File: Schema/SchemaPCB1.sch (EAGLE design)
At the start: 17 parts, among them IC1 ESP32-WROOM-32E_M113EH3200PH3Q, IC2 CP2101-GM, J1 10104110-0001LF

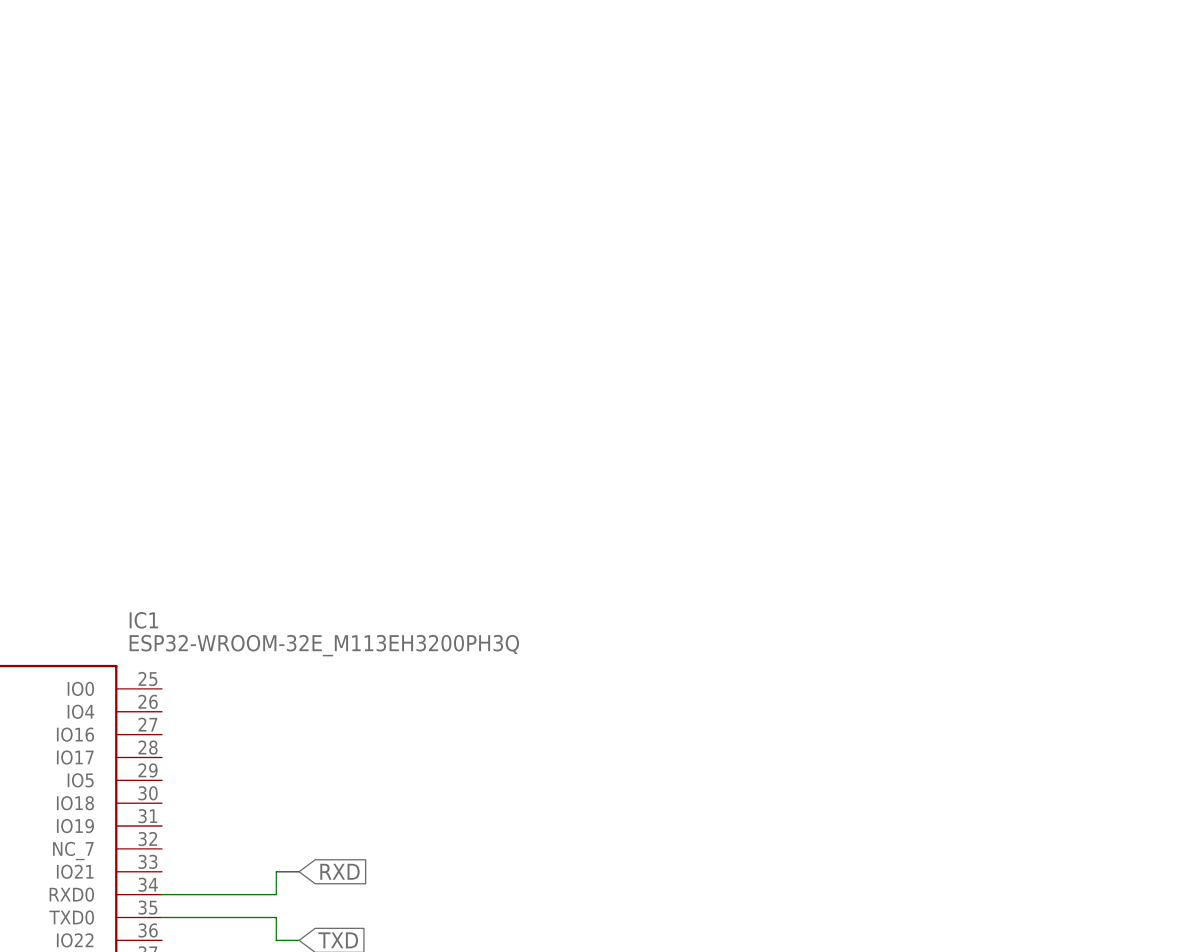
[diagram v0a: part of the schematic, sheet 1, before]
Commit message: LoRa toegevoegd
RN2483 en power voorziening voor de RN2483 aangebracht op het schema
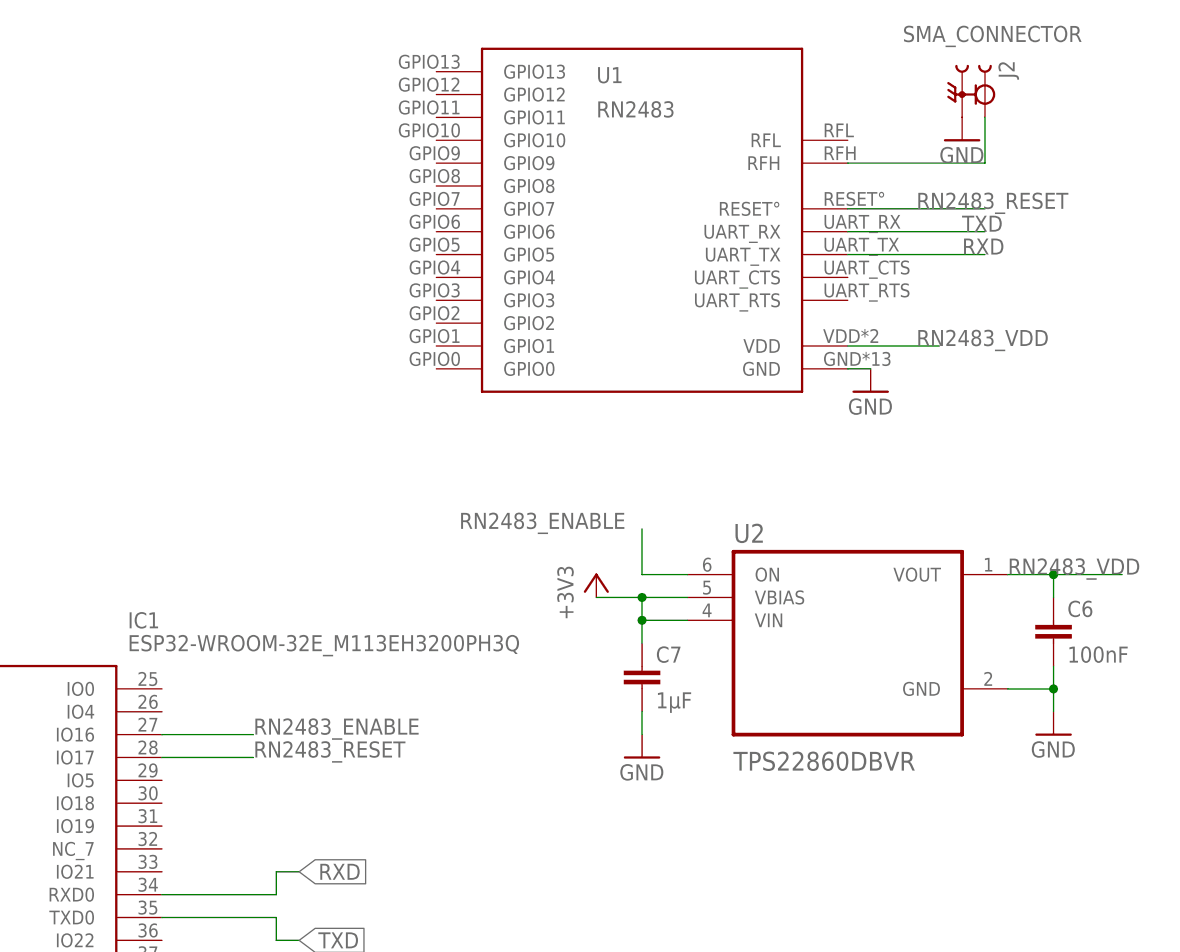
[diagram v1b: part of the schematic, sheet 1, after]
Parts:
- added C6: 100nF, --CoolTeamLib:C-EUC0805
- added C7: 1µF, --CoolTeamLib:C-EUC0805
- added J2: SMA_CONNECTOR, --CoolTeamLib:SMA_CONNECTOR
- added U1: RN2483, --CoolTeamLib:RN2483
- added U2: TPS22860DBVR, --TPS22860DBVR:TPS22860DBVR
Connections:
- new net N$4: J2.1, U1.RFH
- new net RN2483_ENABLE: IC1.IO16, U2.ON
- new net RN2483_RESET: IC1.IO17, U1.RESET°
- new net RN2483_VDD: C6.1, U1.VDD, U2.VOUT
- net +3V3: now also C7.1, U2.VBIAS, U2.VIN
- net GND: now also C6.2, C7.2, J2.2, U1.GND, U2.GND
- net RXD: now also U1.UART_TX
- net TXD: now also U1.UART_RX

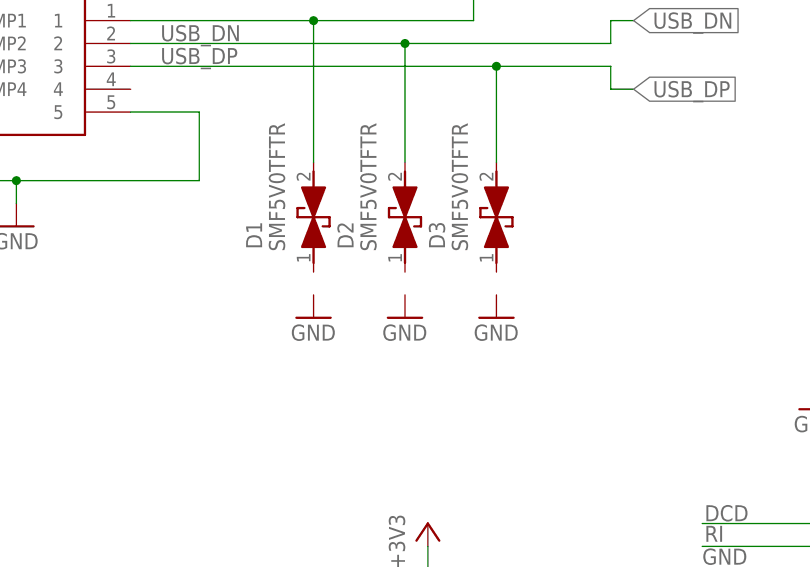
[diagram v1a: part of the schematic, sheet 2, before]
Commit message: buck bom list added
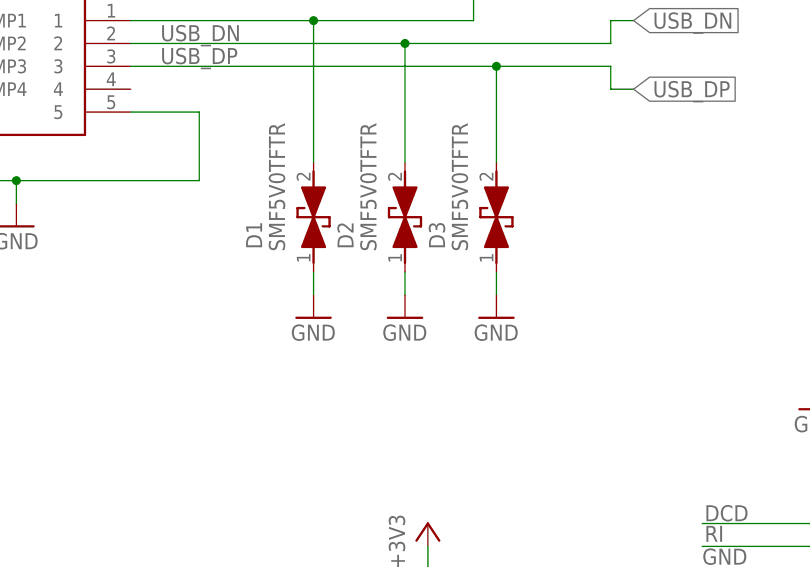
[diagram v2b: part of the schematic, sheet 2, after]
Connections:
- net GND: now also D1.K, D2.K, D3.K
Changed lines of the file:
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@@
 <junction x="50.8" y="165.1"/>
+</segment>
+<segment>
+<pinref part="D1" gate="G$1" pin="K"/>
+<pinref part="GND8" gate="1" pin="GND"/>
+<wire x1="83.82" y1="154.94" x2="83.82" y2="152.4" width="0.1524" layer="91"/>
+</segment>
+<segment>
+<pinref part="D2" gate="G$1" pin="K"/>
+<pinref part="GND9" gate="1" pin="GND"/>
+<wire x1="93.98" y1="154.94" x2="93.98" y2="152.4" width="0.1524" layer="91"/>
+</segment>
+<segment>
+<pinref part="D3" gate="G$1" pin="K"/>
+<pinref part="GND10" gate="1" pin="GND"/>
+<wire x1="104.14" y1="154.94" x2="104.14" y2="152.4" width="0.1524" layer="91"/>
 </segment>
 </net>

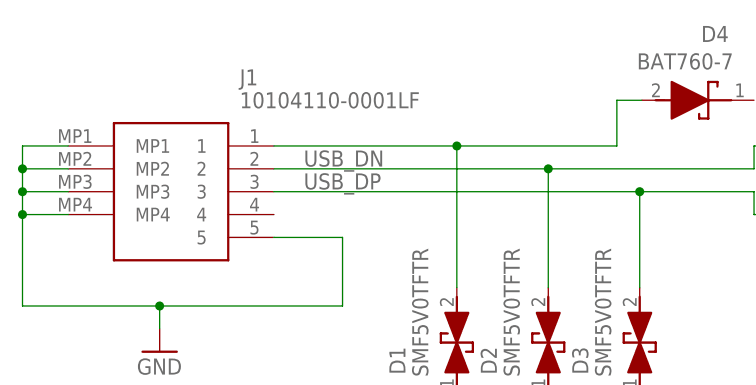
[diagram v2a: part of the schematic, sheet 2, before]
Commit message: buck added (shcema en bom)
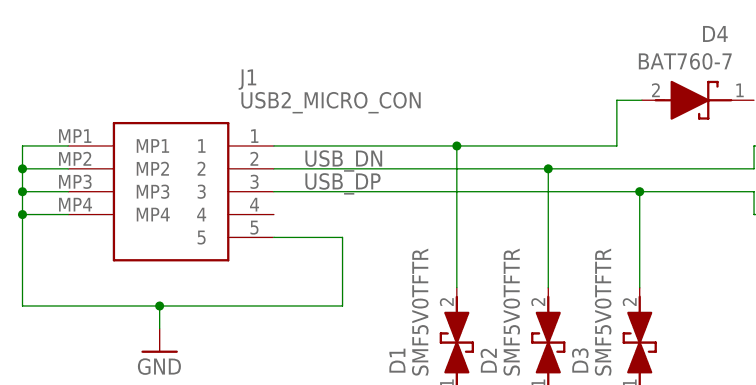
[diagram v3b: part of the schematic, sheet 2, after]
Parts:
- added CBOOT: 100nF, --CoolTeamLib:C-EU-0603C0805
- added CFF: 39pF, --CoolTeamLib:C-EU-0603C0805
- added CIN: 10µF, --CoolTeamLib:C-EU-0805C0805
- added CINX: 100nF, --CoolTeamLib:C-EU-0805C0805
- added COUT: 22µF, --CoolTeamLib:C-EU-0805C0805
- added IC3: TPS563207DRLR, --CoolTeamLib:TPS563207DRLR
- added L1: 3,3µH, --CoolTeamLib:SDR1307-3R3ML
- added R6: 30k9Û, --CoolTeamLib:R-EU_0603M0805
- added R7: 10kÛ, --CoolTeamLib:R-EU_0603M0805
- C1, C2, C4, C6, C7: device --CoolTeamLib:C-EUC0805 -> --CoolTeamLib:C-EU-0805C0805
- J1: value 10104110-0001LF -> USB2_MICRO_CON; device --CoolTeamLib:10104110-0001LF -> --CoolTeamLib:USB2_MICRO_CON
- R1, R2, R3, R4, R5: device --CoolTeamLib:R-EU_M0805 -> --CoolTeamLib:R-EU_0805M0805
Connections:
- new net 3V3: CFF.1, COUT.1, L1.2, R6.2
- new net BAT_IN: CIN.1, CINX.1, IC3.EN, IC3.VIN
- new net N$6: CBOOT.1, IC3.BST
- new net N$7: CBOOT.2, IC3.SW, L1.1
- new net N$8: CFF.2, IC3.FB, R6.1, R7.2
- net GND: now also CIN.2, CINX.2, COUT.2, IC3.GND, R7.1
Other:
- note added: "quantity 2??????"

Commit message: schemaa
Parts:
- removed CBOOT: 100nF, --CoolTeamLib:C-EU-0603C0805
- removed CFF: 39pF, --CoolTeamLib:C-EU-0603C0805
- removed CIN: 10µF, --CoolTeamLib:C-EU-0805C0805
- removed CINX: 100nF, --CoolTeamLib:C-EU-0805C0805
- removed COUT: 22µF, --CoolTeamLib:C-EU-0805C0805
- removed D1, D2, D3: SMF5V0TFTR, --CoolTeamLib:SMF5V0TFTR
- removed D4: BAT760-7, --CoolTeamLib:BAT760-7
- removed IC2: CP2101-GM, --CoolTeamLib:CP2101-GM
- removed IC3: TPS563207DRLR, --CoolTeamLib:TPS563207DRLR
- removed J1: USB2_MICRO_CON, --CoolTeamLib:USB2_MICRO_CON
- removed L1: 3,3µH, --CoolTeamLib:SDR1307-3R3ML
- removed R2: 22k1Û 5%, --CoolTeamLib:R-EU_0805M0805
- removed R3: 47k5Û 5%, --CoolTeamLib:R-EU_0805M0805
- removed R4: 2kÛ 5%, --CoolTeamLib:R-EU_0805M0805
- removed R5: 10kÛ 5%, --CoolTeamLib:R-EU_0805M0805
- removed R6: 30k9Û, --CoolTeamLib:R-EU_0603M0805
- removed R7: 10kÛ, --CoolTeamLib:R-EU_0603M0805
- added U$1: SOT-89-5, --CoolTeamLib:SOT-89-5
- C4: value 0,1µF -> (none)
- C5: value 4,7µF -> (none); device --CoolTeamLib:CPOL-EU153CLV-0605 -> --CoolTeamLib:C-EU-0805C0805
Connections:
- removed net 3V3: CFF.1, COUT.1, L1.2, R6.2
- removed net BAT_IN: CIN.1, CINX.1, IC3.EN, IC3.VIN
- removed net CTS: IC2.CTS
- removed net DCD: IC2.DCD
- removed net DSR: IC2.DSR
- removed net DTR: IC2.DTR
- removed net N$6: CBOOT.1, IC3.BST
- removed net N$7: CBOOT.2, IC3.SW, L1.1
- removed net N$8: CFF.2, IC3.FB, R6.1, R7.2
- removed net N$9: IC2.VBUS, R2.2, R3.2
- removed net RI: IC2.RI
- removed net RST: IC2.!RST, R4.2
- removed net RTS: IC2.RTS
- removed net SUSPEND: IC2.!SUSPEND, R5.2
- removed net USB_DN: D2.A, IC2.D-, J1.2
- removed net USB_DP: D3.A, IC2.D+, J1.3
- removed net VBUS: R2.1
- net +3V3: no longer C4.1, C5.+, IC2.REGIN, IC2.VDD, R4.1
- net GND: no longer C4.2, C5.-, CIN.2, CINX.2, COUT.2, D1.K, D2.K, D3.K, IC2.EP, IC2.GND, IC3.GND, J1.5, J1.MP1, J1.MP2, J1.MP3, J1.MP4, R3.1, R5.1, R7.1
- net N$3: now also U$1.VSS; no longer D1.A, D4.A, J1.1
- net RXD: no longer IC2.RXD
- net TXD: no longer IC2.TXD
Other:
- note removed: "quantity 2??????"

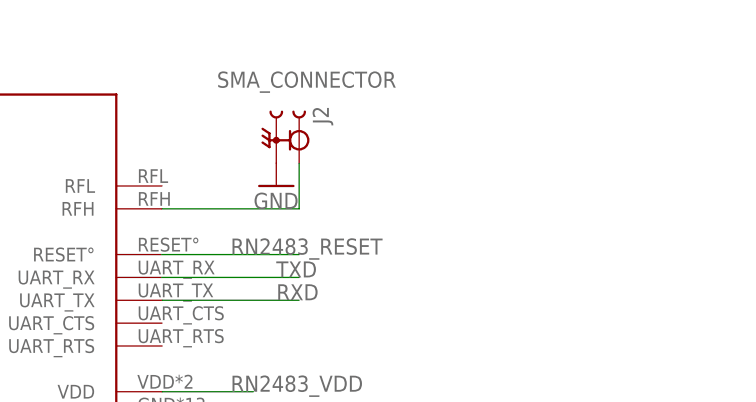
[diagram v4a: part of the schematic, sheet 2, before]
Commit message: LoRa schema afgewerkt
Klaar voor board te maken
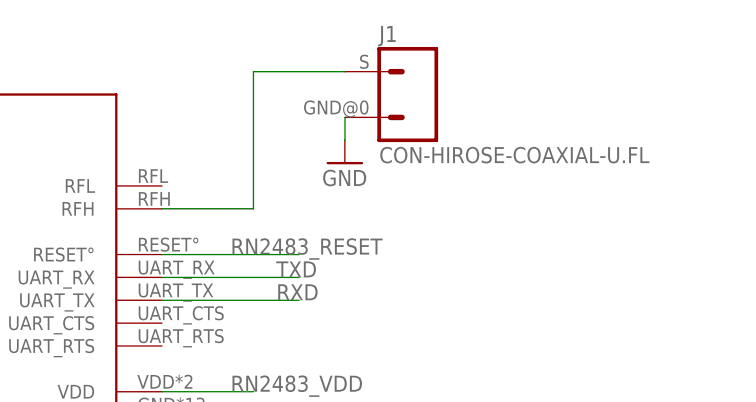
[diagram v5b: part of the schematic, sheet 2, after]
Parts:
- removed J2: SMA_CONNECTOR, --CoolTeamLib:SMA_CONNECTOR
- added J1: CON-HIROSE-COAXIAL-U.FL, --CoolTeamLib:CON-HIROSE-COAXIAL-U.FL
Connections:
- net GND: now also J1.2; no longer J2.2
- net N$4: now also J1.1; no longer J2.1
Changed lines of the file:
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@@
 <drawing>
 <settings>
-<setting alwaysvectorfont="yes"/>
+<setting alwaysvectorfont="no"/>
 <setting keepoldvectorfont="yes"/>
 <setting verticaltext="up"/>
@@
 <part name="GND12" library="supply1" library_urn="urn:adsk.eagle:library:371" deviceset="GND" device=""/>
 <part name="GND13" library="supply1" library_urn="urn:adsk.eagle:library:371" deviceset="GND" device=""/>
-<part name="J2" library="--CoolTeamLib" deviceset="SMA_CONNECTOR" device=""/>
 <part name="GND14" library="supply1" library_urn="urn:adsk.eagle:library:371" deviceset="GND" device=""/>
 <part name="FRAME3" library="frames" library_urn="urn:adsk.eagle:library:229" deviceset="FRAME_A_L" device=""/>
@@
 <part name="C4" library="--CoolTeamLib" deviceset="C-EU-0805" device="C0805" package3d_urn="urn:adsk.eagle:package:23617/2"/>
 <part name="C5" library="--CoolTeamLib" deviceset="C-EU-0805" device="C0805" package3d_urn="urn:adsk.eagle:package:23617/2"/>
+<part name="J1" library="--CoolTeamLib" deviceset="CON-HIROSE-COAXIAL" device="-U.FL"/>
 </parts>
 <sheets>
@@
 <attribute name="VALUE" x="165.1" y="76.2" size="1.778" layer="96"/>
 </instance>
-<instance part="J2" gate="G$1" x="160.02" y="149.86" smashed="yes" rot="R270">
-<attribute name="NAME" x="161.544" y="153.67" size="1.778" layer="95" rot="R270"/>
-<attribute name="VALUE" x="150.876" y="155.702" size="1.778" layer="96"/>
-</instance>
-<instance part="GND14" gate="1" x="157.48" y="144.78" smashed="yes">
-<attribute name="VALUE" x="154.94" y="142.24" size="1.778" layer="96"/>
+<instance part="GND14" gate="1" x="165.1" y="147.32" smashed="yes">
+<attribute name="VALUE" x="162.56" y="144.78" size="1.778" layer="96"/>
+</instance>
+<instance part="J1" gate="G$1" x="172.72" y="154.94" smashed="yes">
+<attribute name="VALUE" x="168.91" y="147.32" size="1.778" layer="96"/>
+<attribute name="NAME" x="168.91" y="160.782" size="1.778" layer="95"/>
 </instance>
 </instances>
@@
 </segment>
 <segment>
-<pinref part="J2" gate="G$1" pin="2"/>
 <pinref part="GND14" gate="1" pin="GND"/>
+<pinref part="J1" gate="G$1" pin="2"/>
+<wire x1="165.1" y1="149.86" x2="165.1" y2="152.4" width="0.1524" layer="91"/>
 </segment>
 </net>
@@
 <segment>
 <pinref part="U1" gate="G$1" pin="RFH"/>
-<wire x1="144.78" y1="142.24" x2="160.02" y2="142.24" width="0.1524" layer="91"/>
-<pinref part="J2" gate="G$1" pin="1"/>
-<wire x1="160.02" y1="142.24" x2="160.02" y2="147.32" width="0.1524" layer="91"/>
-</segment>
-</net>
+<wire x1="144.78" y1="142.24" x2="154.94" y2="142.24" width="0.1524" layer="91"/>
+<wire x1="154.94" y1="142.24" x2="154.94" y2="157.48" width="0.1524" layer="91"/>
+<pinref part="J1" gate="G$1" pin="1"/>
+<wire x1="154.94" y1="157.48" x2="165.1" y2="157.48" width="0.1524" layer="91"/>
+</segment>
+</net>

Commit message: schema dingen
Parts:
- added C8, C9: 100nF, --CoolTeamLib:C-EU-0805C0805
- added J2: Programmer, --CoolTeamLib:CONN_05
- added J3: (no value), --CoolTeamLib:CONN_10"
- added R2, R3: 4k6Û, --CoolTeamLib:R-EU_0805M0805
- added S1, S2: LL3301NF065QG, --CoolTeamLib:LL3301NF065QG
- added U5: SI7217-B-01-IVR, --CoolTeamLib:SI7217-B-01-IVR
- C1, C2: value 0,1µF -> 100nF
- C3: device --CoolTeamLib:CPOL-EU153CLV-0605 -> --CoolTeamLib:VE-220M1VTR-0605
- C4, C5: value (none) -> 1µF
- renumbered IC1 to U3, U$1 to U4
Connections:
- new net BAT_IN: C4.1, U4.V_IN
- new net ESP32_EN: C2.1, C8.2, J2.1, R1.2, S2.2, U3.EN
- new net HALL_DATA: J3.3, U3.SENSOR_VP, U5.OUT1
- new net HALL_EN: J3.4, U3.IO4, U5.DIS
- new net I2C_SCL: R2.1, U3.IO22
- new net I2C_SDA: J3.7, J3.8, R3.1, U3.IO21
- new net IO0: C9.1, S1.2, U3.IO0
- new net RXD0: J2.2, J3.6, U3.RXD0
- new net TXD0: J2.3, J3.5, U3.TXD0
- net +3V3: now also C5.1, J2.5, J3.10, R2.2, R3.2, U4.V_OUT, U5.VDD
- net GND: now also C4.2, C5.2, C8.1, C9.2, J2.4, J3.9, S1.4, S2.4, U4.VSS1, U4.VSS2, U5.GND
- net N$2: now also J3.1; no longer C2.1, R1.2, U3.EN
- net N$3: now also J3.2; no longer U4.VSS
- net RXD: no longer U3.RXD0
- net TXD: no longer U3.TXD0
